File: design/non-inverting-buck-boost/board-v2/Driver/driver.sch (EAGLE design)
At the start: 5 parts

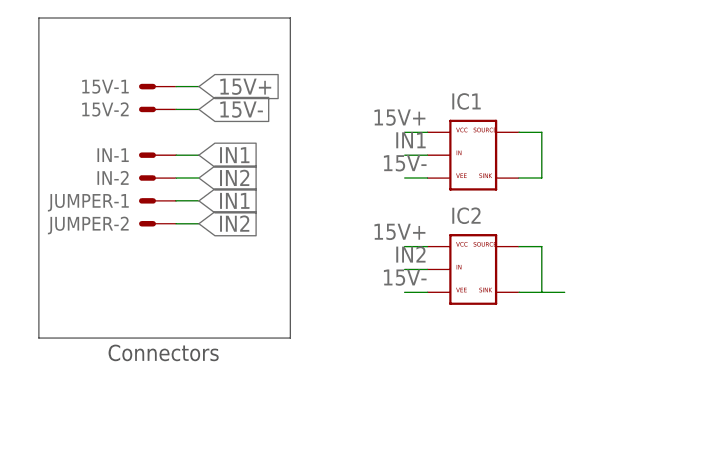
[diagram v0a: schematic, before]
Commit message: finished driver board layout
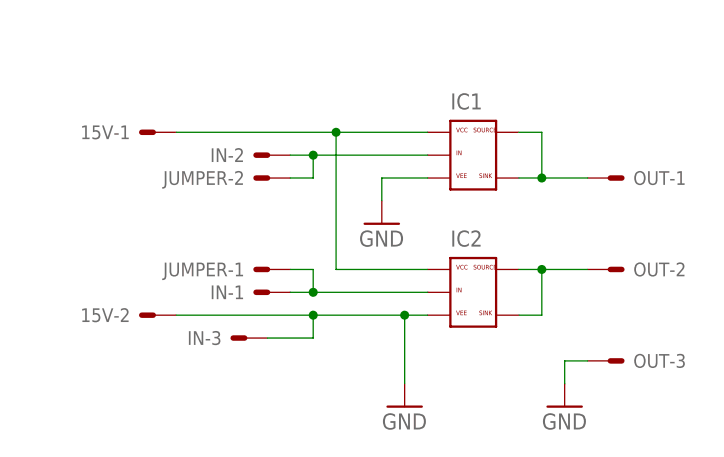
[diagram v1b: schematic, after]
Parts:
- added OUT: 22-23-2031, con-molex:22-23-2031
- IN: value 22-23-2021 -> 22-23-2031; device con-molex:22-23-2021 -> con-molex:22-23-2031
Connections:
- removed net 15V-: 15V-2.S, IC1.VEE, IC2.VEE
- new net GND: 15V-2.S, IC1.VEE, IC2.VEE, IN-3.S, OUT-3.S
- net IN1: now also IC2.IN; no longer IC1.IN
- net IN2: now also IC1.IN; no longer IC2.IN
- net N$5: now also OUT-1.S
- net N$6: now also OUT-2.S
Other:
- note removed: "Connectors"
- moved on the sheet: 15V-1, 15V-2, IC2, IN-1, IN-2, JUMPER-1, JUMPER-2
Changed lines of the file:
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@@
 <parts>
 <part name="15V" library="con-molex" deviceset="22-23-2021" device="" value=""/>
-<part name="IN" library="con-molex" deviceset="22-23-2021" device="" value=""/>
 <part name="JUMPER" library="con-molex" deviceset="22-23-2021" device="" value=""/>
 <part name="IC1" library="felippe" deviceset="ZXGD3006E6" device=""/>
 <part name="IC2" library="felippe" deviceset="ZXGD3006E6" device=""/>
+<part name="GND1" library="supply1" deviceset="GND" device=""/>
+<part name="GND2" library="supply1" deviceset="GND" device=""/>
+<part name="OUT" library="con-molex" deviceset="22-23-2031" device=""/>
+<part name="GND3" library="supply1" deviceset="GND" device=""/>
+<part name="IN" library="con-molex" deviceset="22-23-2031" device=""/>
 </parts>
 <sheets>
 <sheet>
 <plain>
-<text x="-27.94" y="27.94" size="1.778" layer="92">Connectors</text>
 </plain>
 <instances>
-<instance part="15V" gate="-1" x="-22.86" y="58.42" smashed="yes" rot="R180">
-<attribute name="NAME" x="-25.4" y="59.182" size="1.524" layer="95" rot="R180"/>
-<attribute name="VALUE" x="-27.178" y="62.103" size="1.778" layer="96" rot="R180"/>
+<instance part="15V" gate="-1" x="-22.86" y="53.34" smashed="yes" rot="R180">
+<attribute name="NAME" x="-25.4" y="54.102" size="1.524" layer="95" rot="R180"/>
+<attribute name="VALUE" x="-27.178" y="57.023" size="1.778" layer="96" rot="R180"/>
 </instance>
-<instance part="15V" gate="-2" x="-22.86" y="55.88" rot="R180"/>
-<instance part="IN" gate="-1" x="-22.86" y="50.8" smashed="yes" rot="R180">
-<attribute name="NAME" x="-25.4" y="51.562" size="1.524" layer="95" rot="R180"/>
-<attribute name="VALUE" x="-27.178" y="54.483" size="1.778" layer="96" rot="R180"/>
+<instance part="15V" gate="-2" x="-22.86" y="33.02" rot="R180"/>
+<instance part="JUMPER" gate="-1" x="-10.16" y="38.1" rot="R180"/>
+<instance part="JUMPER" gate="-2" x="-10.16" y="48.26" rot="R180"/>
+<instance part="IC1" gate="G$1" x="12.7" y="50.8"/>
+<instance part="IC2" gate="G$1" x="12.7" y="35.56"/>
+<instance part="GND1" gate="1" x="5.08" y="22.86"/>
+<instance part="GND2" gate="1" x="2.54" y="43.18"/>
+<instance part="OUT" gate="-1" x="27.94" y="48.26" smashed="yes">
+<attribute name="NAME" x="30.48" y="47.498" size="1.524" layer="95"/>
 </instance>
-<instance part="IN" gate="-2" x="-22.86" y="48.26" rot="R180"/>
-<instance part="JUMPER" gate="-1" x="-22.86" y="45.72" rot="R180"/>
-<instance part="JUMPER" gate="-2" x="-22.86" y="43.18" rot="R180"/>
-<instance part="IC1" gate="G$1" x="12.7" y="50.8"/>
-<instance part="IC2" gate="G$1" x="12.7" y="38.1"/>
+<instance part="OUT" gate="-2" x="27.94" y="38.1" smashed="yes">
+<attribute name="NAME" x="30.48" y="37.338" size="1.524" layer="95"/>
+</instance>
+<instance part="OUT" gate="-3" x="27.94" y="27.94"/>
+<instance part="GND3" gate="1" x="22.86" y="22.86"/>
+<instance part="IN" gate="-1" x="-10.16" y="35.56" smashed="yes" rot="R180">
+<attribute name="NAME" x="-12.7" y="36.322" size="1.524" layer="95" rot="R180"/>
+</instance>
+<instance part="IN" gate="-2" x="-10.16" y="50.8" rot="R180"/>
+<instance part="IN" gate="-3" x="-12.7" y="30.48" smashed="yes" rot="R180">
+<attribute name="NAME" x="-15.24" y="31.242" size="1.524" layer="95" rot="R180"/>
+</instance>
 </instances>
 <busses>
-<bus name="B$1">
-<segment>
-<wire x1="-35.56" y1="66.04" x2="-7.62" y2="66.04" width="0.762" layer="92"/>
-<wire x1="-7.62" y1="66.04" x2="-7.62" y2="30.48" width="0.762" layer="92"/>
-<wire x1="-7.62" y1="30.48" x2="-35.56" y2="30.48" width="0.762" layer="92"/>
-<wire x1="-35.56" y1="30.48" x2="-35.56" y2="66.04" width="0.762" layer="92"/>
-</segment>
-</bus>
 </busses>
 <nets>
@@
 <pinref part="IC1" gate="G$1" pin="SOURCE"/>
 <pinref part="IC1" gate="G$1" pin="SINK"/>
+<junction x="20.32" y="48.26"/>
+<pinref part="OUT" gate="-1" pin="S"/>
+<wire x1="25.4" y1="48.26" x2="20.32" y2="48.26" width="0.1524" layer="91"/>
 </segment>
 </net>
 <net name="N$6" class="0">
 <segment>
-<wire x1="20.32" y1="40.64" x2="17.78" y2="40.64" width="0.1524" layer="91"/>
-<wire x1="20.32" y1="35.56" x2="20.32" y2="40.64" width="0.1524" layer="91"/>
-<wire x1="17.78" y1="35.56" x2="20.32" y2="35.56" width="0.1524" layer="91"/>
-<wire x1="20.32" y1="35.56" x2="22.86" y2="35.56" width="0.1524" layer="91"/>
+<wire x1="20.32" y1="38.1" x2="17.78" y2="38.1" width="0.1524" layer="91"/>
+<wire x1="20.32" y1="33.02" x2="20.32" y2="38.1" width="0.1524" layer="91"/>
+<wire x1="17.78" y1="33.02" x2="20.32" y2="33.02" width="0.1524" layer="91"/>
 <pinref part="IC2" gate="G$1" pin="SOURCE"/>
 <pinref part="IC2" gate="G$1" pin="SINK"/>
+<pinref part="OUT" gate="-2" pin="S"/>
+<wire x1="25.4" y1="38.1" x2="20.32" y2="38.1" width="0.1524" layer="91"/>
+<junction x="20.32" y="38.1"/>
 </segment>
 </net>
 <net name="15V+" class="0">
 <segment>
+<pinref part="IC2" gate="G$1" pin="VCC"/>
 <pinref part="15V" gate="-1" pin="S"/>
-<wire x1="-20.32" y1="58.42" x2="-17.78" y2="58.42" width="0.1524" layer="91"/>
-<label x="-17.78" y="58.42" size="1.778" layer="95" xref="yes"/>
-</segment>
-<segment>
-<wire x1="7.62" y1="53.34" x2="5.08" y2="53.34" width="0.1524" layer="91"/>
-<label x="7.62" y="55.88" size="1.778" layer="95" rot="R180"/>
+<wire x1="-20.32" y1="53.34" x2="-2.54" y2="53.34" width="0.1524" layer="91"/>
 <pinref part="IC1" gate="G$1" pin="VCC"/>
-</segment>
-<segment>
-<wire x1="7.62" y1="40.64" x2="5.08" y2="40.64" width="0.1524" layer="91"/>
-<label x="7.62" y="43.18" size="1.778" layer="95" rot="R180"/>
-<pinref part="IC2" gate="G$1" pin="VCC"/>
-</segment>
-</net>
-<net name="15V-" class="0">
-<segment>
-<pinref part="15V" gate="-2" pin="S"/>
-<wire x1="-20.32" y1="55.88" x2="-17.78" y2="55.88" width="0.1524" layer="91"/>
-<label x="-17.78" y="55.88" size="1.778" layer="95" xref="yes"/>
-</segment>
-<segment>
-<wire x1="7.62" y1="48.26" x2="5.08" y2="48.26" width="0.1524" layer="91"/>
-<label x="7.62" y="50.8" size="1.778" layer="95" rot="R180"/>
-<pinref part="IC1" gate="G$1" pin="VEE"/>
-</segment>
-<segment>
-<wire x1="7.62" y1="35.56" x2="5.08" y2="35.56" width="0.1524" layer="91"/>
-<label x="7.62" y="38.1" size="1.778" layer="95" rot="R180"/>
-<pinref part="IC2" gate="G$1" pin="VEE"/>
+<wire x1="-2.54" y1="53.34" x2="7.62" y2="53.34" width="0.1524" layer="91"/>
+<wire x1="7.62" y1="38.1" x2="-2.54" y2="38.1" width="0.1524" layer="91"/>
+<wire x1="-2.54" y1="38.1" x2="-2.54" y2="53.34" width="0.1524" layer="91"/>
+<junction x="-2.54" y="53.34"/>
 </segment>
 </net>
 <net name="IN1" class="0">
 <segment>
+<pinref part="JUMPER" gate="-1" pin="S"/>
+<wire x1="-7.62" y1="38.1" x2="-5.08" y2="38.1" width="0.1524" layer="91"/>
+<wire x1="-7.62" y1="35.56" x2="-5.08" y2="35.56" width="0.1524" layer="91"/>
+<wire x1="-5.08" y1="38.1" x2="-5.08" y2="35.56" width="0.1524" layer="91"/>
 <pinref part="IN" gate="-1" pin="S"/>
-<wire x1="-20.32" y1="50.8" x2="-17.78" y2="50.8" width="0.1524" layer="91"/>
-<label x="-17.78" y="50.8" size="1.778" layer="95" xref="yes"/>
-</segment>
-<segment>
-<pinref part="JUMPER" gate="-1" pin="S"/>
-<wire x1="-20.32" y1="45.72" x2="-17.78" y2="45.72" width="0.1524" layer="91"/>
-<label x="-17.78" y="45.72" size="1.778" layer="95" xref="yes"/>
-</segment>
-<segment>
-<wire x1="7.62" y1="50.8" x2="5.08" y2="50.8" width="0.1524" layer="91"/>
-<label x="7.62" y="53.34" size="1.778" layer="95" rot="R180"/>
-<pinref part="IC1" gate="G$1" pin="IN"/>
+<pinref part="IC2" gate="G$1" pin="IN"/>
+<wire x1="-5.08" y1="35.56" x2="7.62" y2="35.56" width="0.1524" layer="91"/>
+<junction x="-5.08" y="35.56"/>
 </segment>
 </net>
 <net name="IN2" class="0">
 <segment>
+<wire x1="-7.62" y1="50.8" x2="-5.08" y2="50.8" width="0.1524" layer="91"/>
+<pinref part="JUMPER" gate="-2" pin="S"/>
+<wire x1="-7.62" y1="48.26" x2="-5.08" y2="48.26" width="0.1524" layer="91"/>
+<wire x1="-5.08" y1="48.26" x2="-5.08" y2="50.8" width="0.1524" layer="91"/>
 <pinref part="IN" gate="-2" pin="S"/>
-<wire x1="-20.32" y1="48.26" x2="-17.78" y2="48.26" width="0.1524" layer="91"/>
-<label x="-17.78" y="48.26" size="1.778" layer="95" xref="yes"/>
+<pinref part="IC1" gate="G$1" pin="IN"/>
+<wire x1="-5.08" y1="50.8" x2="7.62" y2="50.8" width="0.1524" layer="91"/>
+<junction x="-5.08" y="50.8"/>
+</segment>
+</net>
+<net name="GND" class="0">
+<segment>
+<pinref part="IC1" gate="G$1" pin="VEE"/>
+<pinref part="GND2" gate="1" pin="GND"/>
+<wire x1="7.62" y1="48.26" x2="2.54" y2="48.26" width="0.1524" layer="91"/>
+<wire x1="2.54" y1="48.26" x2="2.54" y2="45.72" width="0.1524" layer="91"/>
 </segment>
 <segment>
-<pinref part="JUMPER" gate="-2" pin="S"/>
-<wire x1="-20.32" y1="43.18" x2="-17.78" y2="43.18" width="0.1524" layer="91"/>
-<label x="-17.78" y="43.18" size="1.778" layer="95" xref="yes"/>
+<pinref part="OUT" gate="-3" pin="S"/>
+<pinref part="GND3" gate="1" pin="GND"/>
+<wire x1="25.4" y1="27.94" x2="22.86" y2="27.94" width="0.1524" layer="91"/>
+<wire x1="22.86" y1="27.94" x2="22.86" y2="25.4" width="0.1524" layer="91"/>
 </segment>
 <segment>
-<wire x1="7.62" y1="38.1" x2="5.08" y2="38.1" width="0.1524" layer="91"/>
-<label x="7.62" y="40.64" size="1.778" layer="95" rot="R180"/>
-<pinref part="IC2" gate="G$1" pin="IN"/>
+<pinref part="15V" gate="-2" pin="S"/>
+<pinref part="IC2" gate="G$1" pin="VEE"/>
+<wire x1="-20.32" y1="33.02" x2="-5.08" y2="33.02" width="0.1524" layer="91"/>
+<wire x1="-5.08" y1="33.02" x2="5.08" y2="33.02" width="0.1524" layer="91"/>
+<junction x="-5.08" y="33.02"/>
+<pinref part="IN" gate="-3" pin="S"/>
+<wire x1="5.08" y1="33.02" x2="7.62" y2="33.02" width="0.1524" layer="91"/>
+<wire x1="-5.08" y1="30.48" x2="-5.08" y2="33.02" width="0.1524" layer="91"/>
+<wire x1="-10.16" y1="30.48" x2="-5.08" y2="30.48" width="0.1524" layer="91"/>
+<pinref part="GND1" gate="1" pin="GND"/>
+<wire x1="5.08" y1="25.4" x2="5.08" y2="33.02" width="0.1524" layer="91"/>
+<junction x="5.08" y="33.02"/>
 </segment>
 </net>
